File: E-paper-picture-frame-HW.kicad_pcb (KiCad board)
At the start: 2 copper layers, 93 parts, among them IC1 TPS63001DRCR, J1 Connector, USB-TYPE-C-16P, J2 Conn_01x02, Q1 AO3401A, Q2 BSS138, Q3 AO3401A, Q4 AO3401A, SW1 SS-2235-H2.0, U1 TP4054, U2 ESP32-C6-MINI-1

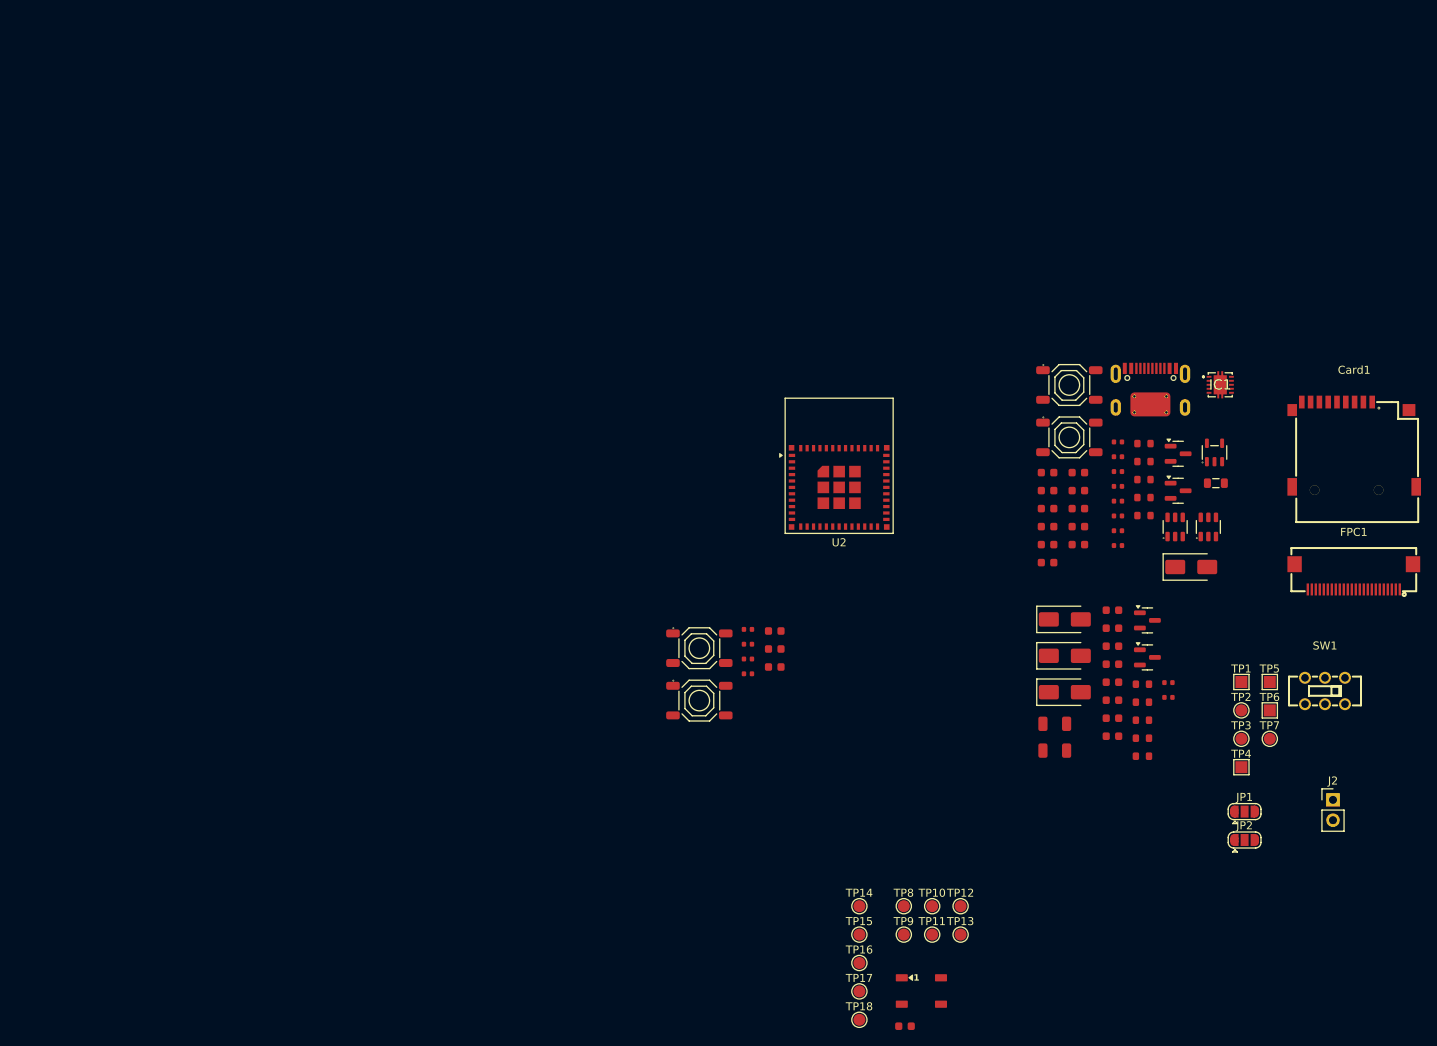
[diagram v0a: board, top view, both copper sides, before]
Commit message: Schematic cleanup and initial layout complete
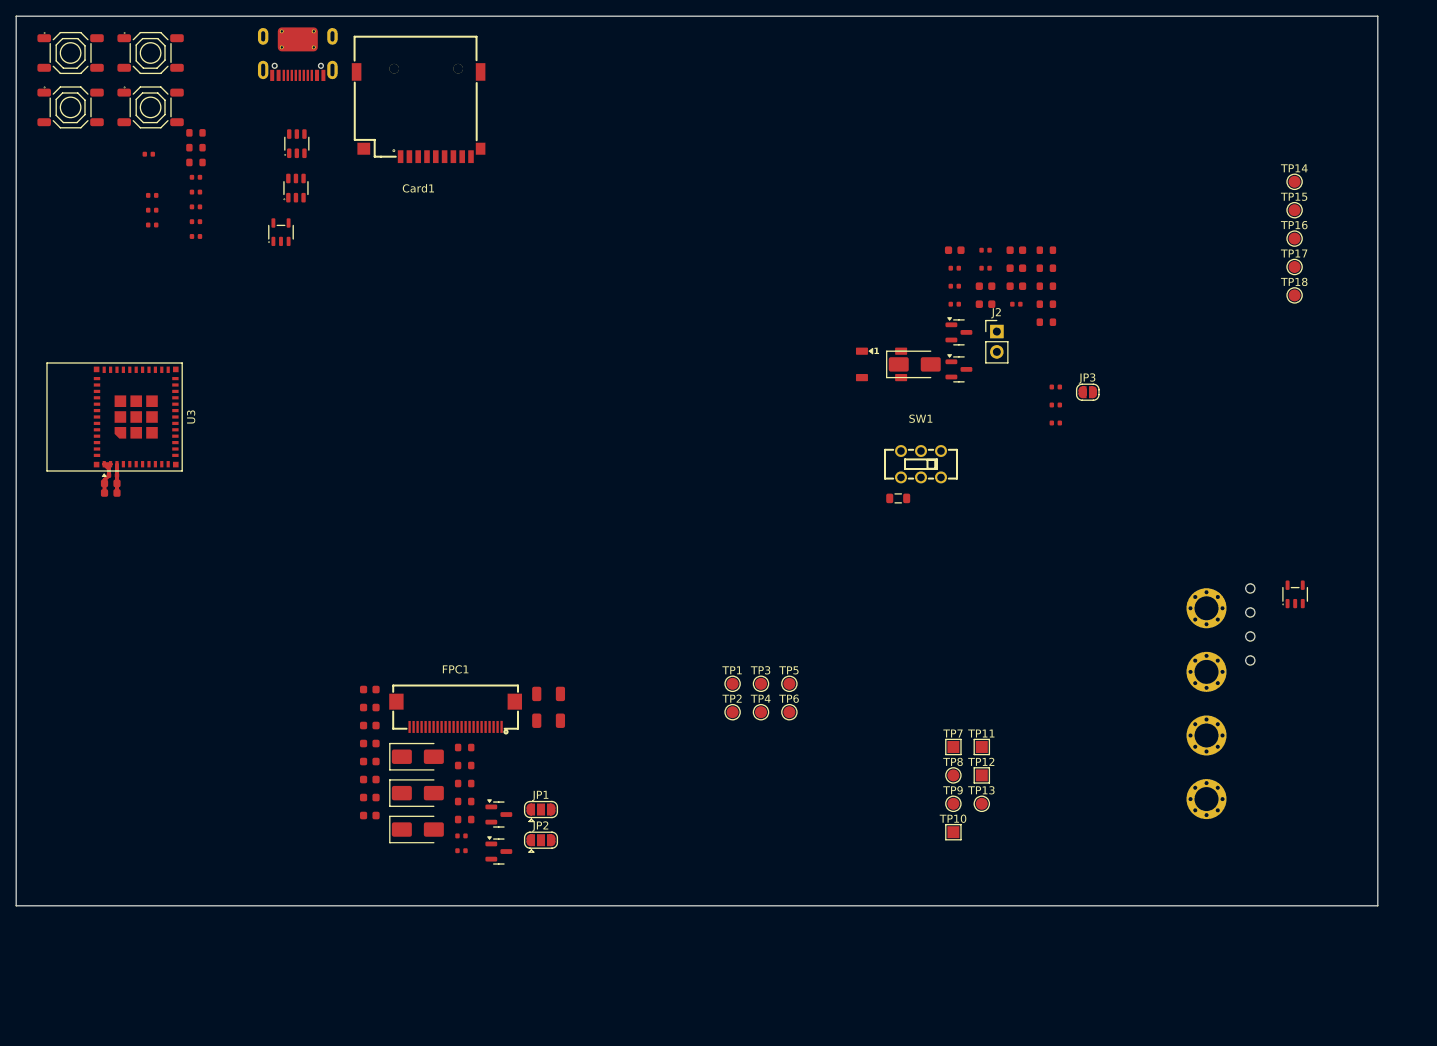
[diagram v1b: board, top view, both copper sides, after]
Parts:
- removed IC1: TPS63001DRCR, Libraries:TPS74901DRCR
- added H1: ~, PCM_JLCPCB:Hole, 3mm, F.Cu at (171.7, 93.5)
- added H2: ~, PCM_JLCPCB:Hole, 3mm, F.Cu at (171.7, 101.5)
- added H3: ~, PCM_JLCPCB:Hole, 3mm, F.Cu at (171.7, 109.4)
- added H4: ~, PCM_JLCPCB:Hole, 3mm, F.Cu at (171.7, 117.4)
- added H5: ~, PCM_JLCPCB:Hole_Tooling_JLCPCB, F.Cu at (177.2, 91.0)
- added H6: ~, PCM_JLCPCB:Hole_Tooling_JLCPCB, F.Cu at (177.2, 94.0)
- added H7: ~, PCM_JLCPCB:Hole_Tooling_JLCPCB, F.Cu at (177.2, 97.0)
- added H8: ~, PCM_JLCPCB:Hole_Tooling_JLCPCB, F.Cu at (177.2, 100.0)
- added JP3: SolderJumper_2_Open, Jumper:SolderJumper-2_P1.3mm_Open_RoundedPad1.0x1.5mm, F.Cu at (156.8, 66.5)
- added R24: 10kΩ, PCM_JLCPCB:R_0402, F.Cu at (152.8, 65.8)
- added R25: 10kΩ, PCM_JLCPCB:R_0402, F.Cu at (152.8, 68.1)
- added R26: 10kΩ, PCM_JLCPCB:R_0402, F.Cu at (152.8, 70.3)
- added U3: ESP32-C6-MINI-1, RF_Module:ESP32-C6-MINI-1, F.Cu at (37.9, 69.6)
- C1: value 4.7uF -> 1uF; footprint PCM_JLCPCB:C_1206 -> PCM_JLCPCB:C_0603
- C12, C13, C14, C16, C26: footprint PCM_JLCPCB:C_0603 -> PCM_JLCPCB:C_0402
- C15: value 10uF -> 100nF; footprint PCM_JLCPCB:C_0603 -> PCM_JLCPCB:C_0402
- C18, C25: value 100nF -> 10uF
- C22: value 1uF -> 100nF
- C23: value 10uF -> 1uF; footprint PCM_JLCPCB:C_0603 -> PCM_JLCPCB:C_0402
- C7: value 1uF -> 4.7uF; footprint PCM_JLCPCB:C_0603 -> PCM_JLCPCB:C_1206
- D5: value SRV05-4_C7420376 -> WS2812B; footprint PCM_JLCPCB:SOT-23-6_L2.9-W1.6-P0.95-LS2.8-BL-1 -> PCM_JLCPCB:LED_WS2812B_PLCC4_5.0x5.0mm_P3.2mm
- D7: value WS2812B -> SRV05-4_C7420376; footprint PCM_JLCPCB:LED_WS2812B_PLCC4_5.0x5.0mm_P3.2mm -> PCM_JLCPCB:SOT-23-6_L2.9-W1.6-P0.95-LS2.8-BL-1
- R10, R11, R9: value 10kΩ -> 10Ω; footprint PCM_JLCPCB:R_0402 -> PCM_JLCPCB:R_0603
- R15: value 1MΩ -> 10kΩ; footprint PCM_JLCPCB:R_0603 -> PCM_JLCPCB:R_0402
- R16: value 1MΩ -> 10Ω
- R17: value 10kΩ -> 1MΩ; footprint PCM_JLCPCB:R_0402 -> PCM_JLCPCB:R_0603
- R18: value 10Ω -> 1MΩ
- TP1: value TestPoint_LIPO -> TestPoint_PREVGH; footprint TestPoint:TestPoint_Pad_1.5x1.5mm -> TestPoint:TestPoint_Pad_D1.5mm
- TP10: value TestPoint_EPD3V3 -> TestPoint_3V3; footprint TestPoint:TestPoint_Pad_D1.5mm -> TestPoint:TestPoint_Pad_1.5x1.5mm
- TP11: value TestPoint_CSB -> TestPoint_VDD; footprint TestPoint:TestPoint_Pad_D1.5mm -> TestPoint:TestPoint_Pad_1.5x1.5mm
- TP12: value TestPoint_EPD_DC -> TestPoint_VDD; footprint TestPoint:TestPoint_Pad_D1.5mm -> TestPoint:TestPoint_Pad_1.5x1.5mm
- TP13: value TestPoint_EPD_RST -> TestPoint_CHRG
- TP14: value TestPoint_EPD_RST -> TestPoint_CS1
- TP15: value TestPoint_EPD_RST -> TestPoint_CS0
- TP16: value TestPoint_EPD_RST -> TestPoint_MOSI
- TP17: value TestPoint_EPD_RST -> TestPoint_MISO
- TP18: value TestPoint_EPD_RST -> TestPoint_SCK
- TP2: value TestPoint_GND -> TestPoint_PREVGL
- TP3: value TestPoint_VINA -> TestPoint_EPD3V3
- TP4: value TestPoint_3V3 -> TestPoint_CSB; footprint TestPoint:TestPoint_Pad_1.5x1.5mm -> TestPoint:TestPoint_Pad_D1.5mm
- TP5: value TestPoint_VDD -> TestPoint_EPD_DC; footprint TestPoint:TestPoint_Pad_1.5x1.5mm -> TestPoint:TestPoint_Pad_D1.5mm
- TP6: value TestPoint_VDD -> TestPoint_EPD_RST; footprint TestPoint:TestPoint_Pad_1.5x1.5mm -> TestPoint:TestPoint_Pad_D1.5mm
- TP7: value TestPoint_CHRG -> TestPoint_LIPO; footprint TestPoint:TestPoint_Pad_D1.5mm -> TestPoint:TestPoint_Pad_1.5x1.5mm
- TP8: value TestPoint_PREVGH -> TestPoint_GND
- TP9: value TestPoint_PREVGL -> TestPoint_VINA
- U1: value TP4054 -> TPS63001DRCR
- U2: value ESP32-C6-MINI-1 -> TP4054; footprint RF_Module:ESP32-C6-MINI-1 -> PCM_JLCPCB:SOT-23-5_L3.0-W1.7-P0.95-LS2.8-BL
- moved D7 131.6 mm to (58.0, 35.4)
- moved S1 131.6 mm to (29.7, 24.1)
- moved S2 124.5 mm to (39.7, 24.1)
- moved Card1 124.0 mm to (73.2, 31.8), turned to 180 degrees
- moved R15 122.2 mm to (45.4, 45.2)
- moved R11 121.6 mm to (45.4, 37.8)
- moved R12 121.6 mm to (45.4, 39.6)
- moved R13 121.6 mm to (45.4, 41.5)
- moved R14 121.6 mm to (45.4, 43.3)
- moved R19 121.6 mm to (45.4, 47.0)
- moved R9 121.6 mm to (45.4, 34.1)
- moved R10 121.6 mm to (45.4, 35.9)
- moved C26 120.6 mm to (35.0, 76.9), turned to 180 degrees
- moved U1 119.9 mm to (56.0, 46.5)
- moved D4 117.8 mm to (57.9, 41.0)
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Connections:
- C1 pad 1: /Display/EPD3V3 -> GNDD
- C1 pad 2: GNDD -> Net-(C1-Pad2)
- C13 pad 1: /IO/USER1 -> Net-(JP3-A)
- C13 pad 2: GNDD -> Net-(D5-VDD)
- C14 pad 1: /IO/VBAT_MON -> /IO/USER1
- C15 pad 1: /IO/VDD(SD) -> /IO/EN
- C16 pad 1: /IO/VDD(SD) -> /IO/VBAT_MON
- C18 pad 1: /IO/EN -> /IO/VDD_EXT
- C19 pad 1: /IO/VDD_EXT -> +3.3V
- C2 pad 1: Net-(C2-Pad1) -> /Display/EPD3V3
- C2 pad 2: Net-(Q2-D) -> GNDD
- C21 pad 1: +3.3V -> /IO/VDD(SD)
- C22 pad 1: /MCU/EN -> /IO/VDD(SD)
- C23 pad 1: +3.3V -> /MCU/EN
- C26 pad 1: /IO/VDD(SD) -> +3.3V
- C26 pad 2: Net-(D7-VDD) -> GNDD
- C3 pad 1: GNDD -> /Display/EPD3V3
- C3 pad 2: Net-(C3-Pad2) -> GNDD
- C4 pad 1: /Display/EPD3V3 -> Net-(C4-Pad1)
- C6 pad 1: Net-(C6-Pad1) -> /Display/PREVGH
- C7 pad 1: /Display/PREVGH -> Net-(C7-Pad1)
- C7 pad 2: GNDD -> Net-(Q2-D)
- D1 pad 2: Net-(C2-Pad1) -> Net-(C7-Pad1)
- D2 pad 1: Net-(C2-Pad1) -> Net-(C7-Pad1)
- D4 pad 1: /IO/D- -> /IO/USB D-
- D4 pad 3: /IO/D+ -> /IO/USB D+
- D5 pad 1: /Display/SPI.SCK -> Net-(D5-VDD)
- D5 pad 2: GNDD -> unconnected-(D5-DOUT-Pad2)
- D5 pad 3: /Display/SPI.MOSI -> GNDD
- D5 pad 4: /IO/CS -> Net-(D5-DIN)
- D7 pad 1: Net-(D7-VDD) -> /Display/SPI.SCK
- D7 pad 2: unconnected-(D7-DOUT-Pad2) -> GNDD
- D7 pad 3: GNDD -> /Display/SPI.MOSI
- D7 pad 4: /IO/LED_IN -> /IO/CS
- FPC1 pad 18: Net-(C5-Pad1) -> Net-(C4-Pad1)
- FPC1 pad 20: Net-(C6-Pad1) -> Net-(C5-Pad1)
- FPC1 pad 5: Net-(C3-Pad2) -> Net-(C1-Pad2)
- J1 pad A5: Net-(J1-CC1) -> /IO/USBCC1
- J1 pad A6: /IO/D+ -> /IO/USB D+
- J1 pad A7: /IO/D- -> /IO/USB D-
- J1 pad B5: Net-(J1-CC2) -> /IO/USBCC2
- J1 pad B6: /IO/D+ -> /IO/USB D+
- J1 pad B7: /IO/D- -> /IO/USB D-
- Q3 pad 1: /IO/SD3V3_EN -> /IO/5V_USB
- Q3 pad 2: +3.3V -> /IO/BAT+
- Q3 pad 3: /IO/VDD(SD) -> /IO/VDD_EXT_OPEN
- Q4 pad 1: /IO/5V_USB -> /IO/SD3V3_EN
- Q4 pad 2: /IO/BAT+ -> +3.3V
- Q4 pad 3: /IO/VDD_EXT_OPEN -> /IO/VDD(SD)
- R10 pad 1: Net-(J1-CC2) -> Net-(R10-Pad1)
- R10 pad 2: GNDD -> Net-(R10-Pad2)
- R11 pad 1: Net-(J1-CC1) -> Net-(R10-Pad2)
- R11 pad 2: GNDD -> Net-(D5-DIN)
- R12 pad 1: Net-(J1-CC1) -> /IO/USBCC2
- R13 pad 1: +3.3V -> /IO/USBCC2
- R13 pad 2: /IO/DAT2 -> GNDD
- R14 pad 1: +3.3V -> /IO/USBCC1
- R14 pad 2: /IO/DAT1 -> GNDD
- R15 pad 1: /IO/BAT+ -> /IO/USBCC1
- R15 pad 2: /IO/VBAT_MON -> GNDD
- R16 pad 1: /IO/VBAT_MON -> /IO/VDD_EXT
- R16 pad 2: GNDD -> /IO/EN
- R17 pad 1: +3.3V -> /IO/BAT+
- R17 pad 2: /IO/SD3V3_EN -> /IO/VBAT_MON
- R18 pad 1: /IO/VDD_EXT -> /IO/VBAT_MON
- R18 pad 2: /IO/EN -> GNDD
- R19 pad 1: Net-(U1-PROG) -> Net-(U2-PROG)
- R21 pad 2: /MCU/EN -> /IO/DAT2
- R22 pad 2: /MCU/GPIO9 -> /IO/DAT1
- R23 pad 2: /MCU/GPIO8 -> /IO/SD3V3_EN
- R9 pad 1: Net-(J1-CC2) -> /IO/LED_IN
- R9 pad 2: GNDD -> Net-(R10-Pad1)
- TP1 pad 1: /IO/BAT+ -> /Display/PREVGH
- TP10 pad 1: /Display/EPD3V3 -> +3.3V
- TP11 pad 1: /Display/EPD BUSY(CSB) -> /IO/VDD_EXT
- TP12 pad 1: /Display/EPD DC -> /IO/VDD_EXT_OPEN
- TP13 pad 1: /Display/EPD RST -> /IO/CHRG
- TP14 pad 1: /Display/SPI.MOSI -> /IO/CS
- TP15 pad 1: /MCU/SPI2.MISO -> /Display/EPD CS
- TP16 pad 1: /Display/SPI.SCK -> /Display/SPI.MOSI
- TP17 pad 1: /Display/EPD CS -> /MCU/SPI2.MISO
- TP18 pad 1: /IO/CS -> /Display/SPI.SCK
- TP2 pad 1: GNDD -> /Display/PREVGL
- TP3 pad 1: /IO/EN -> /Display/EPD3V3
- TP4 pad 1: +3.3V -> /Display/EPD BUSY(CSB)
- TP5 pad 1: /IO/VDD_EXT -> /Display/EPD DC
- TP6 pad 1: /IO/VDD_EXT_OPEN -> /Display/EPD RST
- TP7 pad 1: /IO/CHRG -> /IO/BAT+
- TP8 pad 1: /Display/PREVGH -> GNDD
- TP9 pad 1: /Display/PREVGL -> /IO/EN
- U1 pad 1: /IO/CHRG -> unconnected-(U1-VOUT-Pad1)
- U1 pad 2: GNDD -> /IO/L2
- U1 pad 3: /IO/BAT+ -> GNDD
- U1 pad 4: /IO/5V_USB -> /IO/L1
- U1 pad 5: Net-(U1-PROG) -> /IO/VDD_EXT
- U2 pad 1: GNDD -> /IO/CHRG
- U2 pad 3: +3.3V -> /IO/BAT+
- U2 pad 4: unconnected-(U2-NC-Pad4) -> /IO/5V_USB
- U2 pad 5: /IO/USER1 -> Net-(U2-PROG)
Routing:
- net GNDD: track 0.00 -> 5.56 mm
- net +3.3V: track 0.00 -> 3.60 mm
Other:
- board outline added: 170.2 x 111.2 mm
- copper layers 2 -> 4
- rule pad_to_mask_clearance: 0 -> 0.1

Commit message: Small cleanup + linked jlcpcb parts for ordering
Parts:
- added L1: SMNR5040-100MT, Libraries:IND-SMD_2P-L5.0-W5.0, F.Cu at (73.4, 82.3)
- U1: footprint PCM_JLCPCB:SOT-23-5_L3.0-W1.7-P0.95-LS2.8-BL -> Libraries:VSON-10_L3.0-W3.0-P0.50-TL-EP_TPS62410DRCR
- moved U3 15.4 mm to (28.4, 57.4)
- moved C1 12.7 mm to (67.8, 91.0)
- moved C10 12.7 mm to (67.8, 106.8)
- moved C3 12.7 mm to (67.8, 93.3)
- moved C4 12.7 mm to (67.8, 95.5)
- moved C5 12.7 mm to (67.8, 97.8)
- moved C6 12.7 mm to (67.8, 100.0)
- moved C8 12.7 mm to (67.8, 102.3)
- moved C9 12.7 mm to (67.8, 104.5)
- moved R3 12.7 mm to (79.7, 98.3)
- moved R4 12.7 mm to (79.7, 100.5)
- moved R5 12.7 mm to (79.7, 102.8)
- moved R6 12.7 mm to (79.7, 105.0)
- moved R7 12.7 mm to (79.7, 107.3)
- moved C2 12.7 mm to (90.2, 91.6)
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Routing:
- net GNDD: track 5.56 -> 0.00 mm
- net +3.3V: track 3.60 -> 0.00 mm
